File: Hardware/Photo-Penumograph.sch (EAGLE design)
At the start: 49 parts, among them SW1 SWITCH.JS202011JCQN

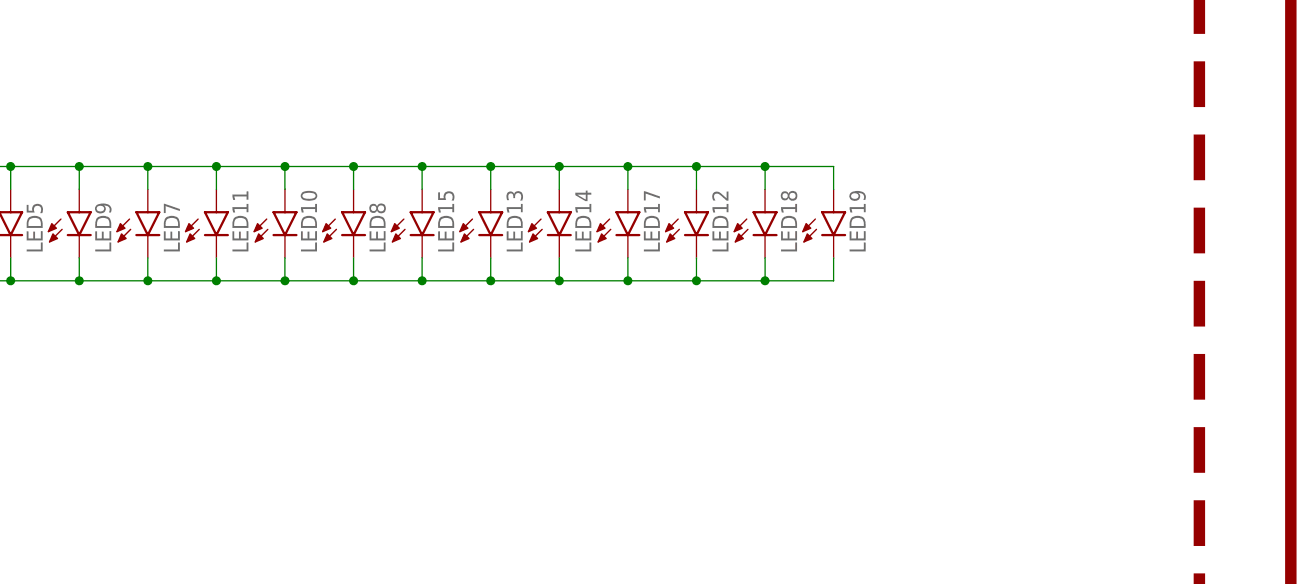
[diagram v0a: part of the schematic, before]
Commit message: Inital lung idea, doesn't expand with breath.
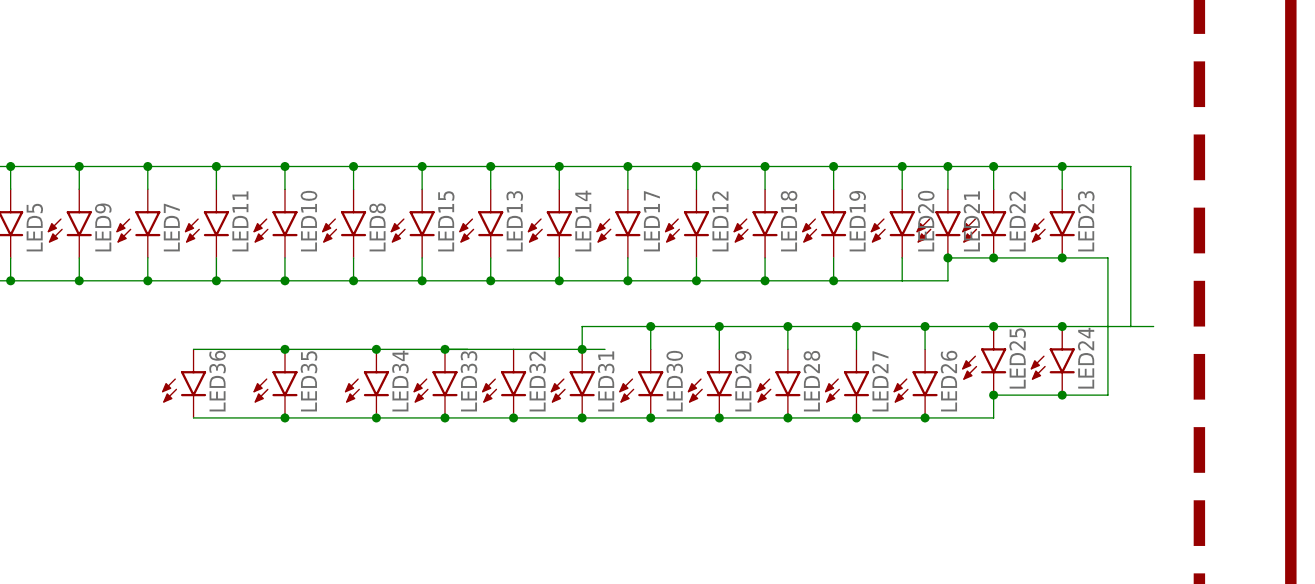
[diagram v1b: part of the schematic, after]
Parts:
- added LED20, LED21, LED22, LED23, LED24, LED25, LED26, LED27, LED28, LED29, LED30, LED31, LED32, LED33, LED34, LED35, LED36: (no value), SparkFun-LED:LED5MM
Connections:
- net ANODE: now also LED20.A, LED21.A, LED22.A, LED23.A, LED24.A, LED25.A, LED26.A, LED27.A, LED28.A, LED29.A, LED30.A, LED32.A, LED33.A, LED34.A, LED35.A, LED36.A
- net GND: now also LED20.C, LED21.C, LED22.C, LED23.C, LED24.C, LED25.C, LED26.C, LED27.C, LED28.C, LED29.C, LED30.C, LED31.C, LED32.C, LED33.C, LED34.C, LED35.C, LED36.C
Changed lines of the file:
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@@
 <?xml version="1.0" encoding="utf-8"?>
 <!DOCTYPE eagle SYSTEM "eagle.dtd">
-<eagle version="8.2.1">
+<eagle version="8.2.0">
 <drawing>
 <settings>
@@
 <part name="SUPPLY6" library="CalvEngIO-Symbols" deviceset="3.3V" device=""/>
 <part name="SUPPLY7" library="CalvEngIO-Symbols" deviceset="3.3V" device=""/>
+<part name="LED20" library="SparkFun-LED" deviceset="LED" device="5MM"/>
+<part name="LED21" library="SparkFun-LED" deviceset="LED" device="5MM"/>
+<part name="LED22" library="SparkFun-LED" deviceset="LED" device="5MM"/>
+<part name="LED23" library="SparkFun-LED" deviceset="LED" device="5MM"/>
+<part name="LED24" library="SparkFun-LED" deviceset="LED" device="5MM"/>
+<part name="LED25" library="SparkFun-LED" deviceset="LED" device="5MM"/>
+<part name="LED26" library="SparkFun-LED" deviceset="LED" device="5MM"/>
+<part name="LED27" library="SparkFun-LED" deviceset="LED" device="5MM"/>
+<part name="LED28" library="SparkFun-LED" deviceset="LED" device="5MM"/>
+<part name="LED29" library="SparkFun-LED" deviceset="LED" device="5MM"/>
+<part name="LED30" library="SparkFun-LED" deviceset="LED" device="5MM"/>
+<part name="LED31" library="SparkFun-LED" deviceset="LED" device="5MM"/>
+<part name="LED32" library="SparkFun-LED" deviceset="LED" device="5MM"/>
+<part name="LED33" library="SparkFun-LED" deviceset="LED" device="5MM"/>
+<part name="LED34" library="SparkFun-LED" deviceset="LED" device="5MM"/>
+<part name="LED35" library="SparkFun-LED" deviceset="LED" device="5MM"/>
+<part name="LED36" library="SparkFun-LED" deviceset="LED" device="5MM"/>
 </parts>
 <sheets>
@@
 <instance part="SUPPLY6" gate="G$1" x="7.62" y="93.98"/>
 <instance part="SUPPLY7" gate="G$1" x="35.56" y="91.44"/>
+<instance part="LED20" gate="G$1" x="358.14" y="73.66"/>
+<instance part="LED21" gate="G$1" x="363.22" y="73.66"/>
+<instance part="LED22" gate="G$1" x="368.3" y="73.66"/>
+<instance part="LED23" gate="G$1" x="375.92" y="73.66"/>
+<instance part="LED24" gate="G$1" x="375.92" y="58.42"/>
+<instance part="LED25" gate="G$1" x="368.3" y="58.42"/>
+<instance part="LED26" gate="G$1" x="360.68" y="55.88"/>
+<instance part="LED27" gate="G$1" x="353.06" y="55.88"/>
+<instance part="LED28" gate="G$1" x="345.44" y="55.88"/>
+<instance part="LED29" gate="G$1" x="337.82" y="55.88"/>
+<instance part="LED30" gate="G$1" x="330.2" y="55.88"/>
+<instance part="LED31" gate="G$1" x="322.58" y="55.88"/>
+<instance part="LED32" gate="G$1" x="314.96" y="55.88"/>
+<instance part="LED33" gate="G$1" x="307.34" y="55.88"/>
+<instance part="LED34" gate="G$1" x="299.72" y="55.88"/>
+<instance part="LED35" gate="G$1" x="289.56" y="55.88"/>
+<instance part="LED36" gate="G$1" x="279.4" y="55.88"/>
 </instances>
 <busses>
@@
 <wire x1="220.98" y1="58.42" x2="220.98" y2="66.04" width="0.1524" layer="91"/>
 <junction x="220.98" y="66.04"/>
+<pinref part="LED20" gate="G$1" pin="C"/>
+<wire x1="358.14" y1="68.58" x2="358.14" y2="66.04" width="0.1524" layer="91"/>
+<junction x="350.52" y="66.04"/>
+<wire x1="358.14" y1="66.04" x2="350.52" y2="66.04" width="0.1524" layer="91"/>
+<wire x1="363.22" y1="66.04" x2="358.14" y2="66.04" width="0.1524" layer="91"/>
+<pinref part="LED24" gate="G$1" pin="C"/>
+<wire x1="375.92" y1="53.34" x2="381" y2="53.34" width="0.1524" layer="91"/>
+<wire x1="381" y1="53.34" x2="381" y2="68.58" width="0.1524" layer="91"/>
+<pinref part="LED23" gate="G$1" pin="C"/>
+<wire x1="381" y1="68.58" x2="375.92" y2="68.58" width="0.1524" layer="91"/>
+<pinref part="LED22" gate="G$1" pin="C"/>
+<wire x1="375.92" y1="68.58" x2="368.3" y2="68.58" width="0.1524" layer="91"/>
+<junction x="375.92" y="68.58"/>
+<pinref part="LED21" gate="G$1" pin="C"/>
+<wire x1="368.3" y1="68.58" x2="363.22" y2="68.58" width="0.1524" layer="91"/>
+<junction x="368.3" y="68.58"/>
+<wire x1="363.22" y1="66.04" x2="363.22" y2="68.58" width="0.1524" layer="91"/>
+<junction x="363.22" y="68.58"/>
+<pinref part="LED25" gate="G$1" pin="C"/>
+<wire x1="375.92" y1="53.34" x2="368.3" y2="53.34" width="0.1524" layer="91"/>
+<junction x="375.92" y="53.34"/>
+<wire x1="368.3" y1="53.34" x2="368.3" y2="50.8" width="0.1524" layer="91"/>
+<junction x="368.3" y="53.34"/>
+<pinref part="LED26" gate="G$1" pin="C"/>
+<wire x1="368.3" y1="50.8" x2="360.68" y2="50.8" width="0.1524" layer="91"/>
+<pinref part="LED27" gate="G$1" pin="C"/>
+<wire x1="360.68" y1="50.8" x2="353.06" y2="50.8" width="0.1524" layer="91"/>
+<junction x="360.68" y="50.8"/>
+<pinref part="LED28" gate="G$1" pin="C"/>
+<wire x1="353.06" y1="50.8" x2="345.44" y2="50.8" width="0.1524" layer="91"/>
+<junction x="353.06" y="50.8"/>
+<pinref part="LED29" gate="G$1" pin="C"/>
+<wire x1="345.44" y1="50.8" x2="337.82" y2="50.8" width="0.1524" layer="91"/>
+<junction x="345.44" y="50.8"/>
+<pinref part="LED30" gate="G$1" pin="C"/>
+<wire x1="337.82" y1="50.8" x2="330.2" y2="50.8" width="0.1524" layer="91"/>
+<junction x="337.82" y="50.8"/>
+<pinref part="LED31" gate="G$1" pin="C"/>
+<wire x1="330.2" y1="50.8" x2="322.58" y2="50.8" width="0.1524" layer="91"/>
+<junction x="330.2" y="50.8"/>
+<pinref part="LED32" gate="G$1" pin="C"/>
+<wire x1="322.58" y1="50.8" x2="314.96" y2="50.8" width="0.1524" layer="91"/>
+<junction x="322.58" y="50.8"/>
+<pinref part="LED33" gate="G$1" pin="C"/>
+<wire x1="314.96" y1="50.8" x2="307.34" y2="50.8" width="0.1524" layer="91"/>
+<junction x="314.96" y="50.8"/>
+<pinref part="LED34" gate="G$1" pin="C"/>
+<wire x1="307.34" y1="50.8" x2="299.72" y2="50.8" width="0.1524" layer="91"/>
+<junction x="307.34" y="50.8"/>
+<pinref part="LED35" gate="G$1" pin="C"/>
+<wire x1="299.72" y1="50.8" x2="289.56" y2="50.8" width="0.1524" layer="91"/>
+<junction x="299.72" y="50.8"/>
+<pinref part="LED36" gate="G$1" pin="C"/>
+<wire x1="289.56" y1="50.8" x2="279.4" y2="50.8" width="0.1524" layer="91"/>
+<junction x="289.56" y="50.8"/>
 </segment>
 <segment>
@@
 <wire x1="220.98" y1="81.28" x2="220.98" y2="78.74" width="0.1524" layer="91"/>
 <junction x="220.98" y="78.74"/>
+<pinref part="LED20" gate="G$1" pin="A"/>
+<wire x1="350.52" y1="78.74" x2="358.14" y2="78.74" width="0.1524" layer="91"/>
+<wire x1="358.14" y1="78.74" x2="358.14" y2="76.2" width="0.1524" layer="91"/>
+<junction x="350.52" y="78.74"/>
+<pinref part="LED21" gate="G$1" pin="A"/>
+<wire x1="363.22" y1="76.2" x2="363.22" y2="78.74" width="0.1524" layer="91"/>
+<wire x1="363.22" y1="78.74" x2="358.14" y2="78.74" width="0.1524" layer="91"/>
+<junction x="358.14" y="78.74"/>
+<pinref part="LED22" gate="G$1" pin="A"/>
+<wire x1="368.3" y1="76.2" x2="368.3" y2="78.74" width="0.1524" layer="91"/>
+<wire x1="368.3" y1="78.74" x2="363.22" y2="78.74" width="0.1524" layer="91"/>
+<junction x="363.22" y="78.74"/>
+<pinref part="LED23" gate="G$1" pin="A"/>
+<wire x1="375.92" y1="76.2" x2="375.92" y2="78.74" width="0.1524" layer="91"/>
+<wire x1="375.92" y1="78.74" x2="368.3" y2="78.74" width="0.1524" layer="91"/>
+<junction x="368.3" y="78.74"/>
+<pinref part="LED24" gate="G$1" pin="A"/>
+<wire x1="375.92" y1="60.96" x2="383.54" y2="60.96" width="0.1524" layer="91"/>
+<wire x1="386.08" y1="60.96" x2="383.54" y2="60.96" width="0.1524" layer="91"/>
+<wire x1="383.54" y1="60.96" x2="383.54" y2="78.74" width="0.1524" layer="91"/>
+<wire x1="383.54" y1="78.74" x2="375.92" y2="78.74" width="0.1524" layer="91"/>
+<junction x="375.92" y="78.74"/>
+<pinref part="LED25" gate="G$1" pin="A"/>
+<wire x1="368.3" y1="60.96" x2="375.92" y2="60.96" width="0.1524" layer="91"/>
+<junction x="375.92" y="60.96"/>
+<pinref part="LED26" gate="G$1" pin="A"/>
+<wire x1="360.68" y1="58.42" x2="360.68" y2="60.96" width="0.1524" layer="91"/>
+<wire x1="360.68" y1="60.96" x2="368.3" y2="60.96" width="0.1524" layer="91"/>
+<junction x="368.3" y="60.96"/>
+<pinref part="LED27" gate="G$1" pin="A"/>
+<wire x1="353.06" y1="58.42" x2="353.06" y2="60.96" width="0.1524" layer="91"/>
+<wire x1="353.06" y1="60.96" x2="360.68" y2="60.96" width="0.1524" layer="91"/>
+<junction x="360.68" y="60.96"/>
+<pinref part="LED28" gate="G$1" pin="A"/>
+<wire x1="345.44" y1="58.42" x2="345.44" y2="60.96" width="0.1524" layer="91"/>
+<wire x1="345.44" y1="60.96" x2="353.06" y2="60.96" width="0.1524" layer="91"/>
+<junction x="353.06" y="60.96"/>
+<pinref part="LED29" gate="G$1" pin="A"/>
+<wire x1="337.82" y1="58.42" x2="337.82" y2="60.96" width="0.1524" layer="91"/>
+<wire x1="337.82" y1="60.96" x2="345.44" y2="60.96" width="0.1524" layer="91"/>
+<junction x="345.44" y="60.96"/>
+<pinref part="LED30" gate="G$1" pin="A"/>
+<wire x1="330.2" y1="58.42" x2="330.2" y2="60.96" width="0.1524" layer="91"/>
+<wire x1="330.2" y1="60.96" x2="337.82" y2="60.96" width="0.1524" layer="91"/>
+<junction x="337.82" y="60.96"/>
+<pinref part="LED36" gate="G$1" pin="A"/>
+<pinref part="LED35" gate="G$1" pin="A"/>
+<wire x1="279.4" y1="58.42" x2="289.56" y2="58.42" width="0.1524" layer="91"/>
+<pinref part="LED34" gate="G$1" pin="A"/>
+<wire x1="289.56" y1="58.42" x2="299.72" y2="58.42" width="0.1524" layer="91"/>
+<junction x="289.56" y="58.42"/>
+<wire x1="299.72" y1="58.42" x2="307.34" y2="58.42" width="0.1524" layer="91"/>
+<junction x="299.72" y="58.42"/>
+<pinref part="LED33" gate="G$1" pin="A"/>
+<wire x1="309.88" y1="58.42" x2="307.34" y2="58.42" width="0.1524" layer="91"/>
+<junction x="307.34" y="58.42"/>
+<pinref part="LED32" gate="G$1" pin="A"/>
+<wire x1="314.96" y1="58.42" x2="322.58" y2="58.42" width="0.1524" layer="91"/>
+<wire x1="322.58" y1="58.42" x2="325.12" y2="58.42" width="0.1524" layer="91"/>
+<wire x1="314.96" y1="58.42" x2="307.34" y2="58.42" width="0.1524" layer="91"/>
+<wire x1="322.58" y1="58.42" x2="322.58" y2="60.96" width="0.1524" layer="91"/>
+<junction x="322.58" y="58.42"/>
+<wire x1="322.58" y1="60.96" x2="330.2" y2="60.96" width="0.1524" layer="91"/>
+<junction x="330.2" y="60.96"/>
 </segment>
 </net>

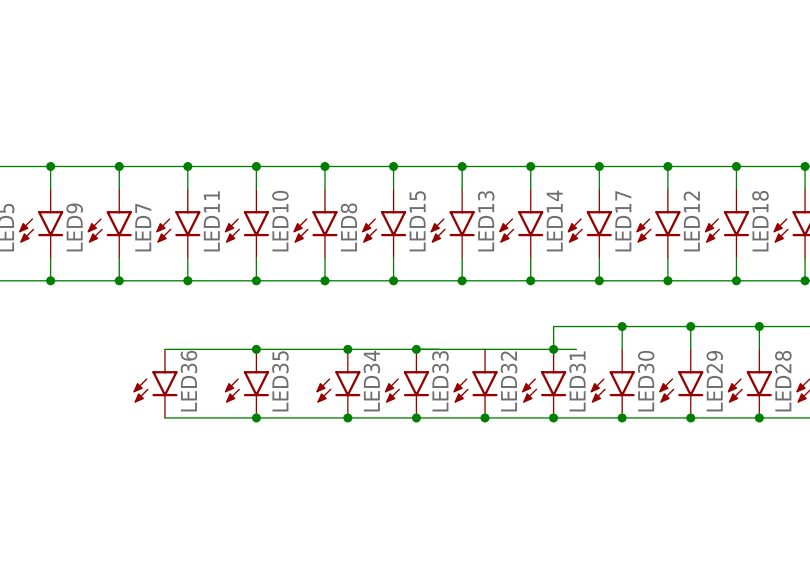
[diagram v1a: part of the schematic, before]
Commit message: Improved basic lung design
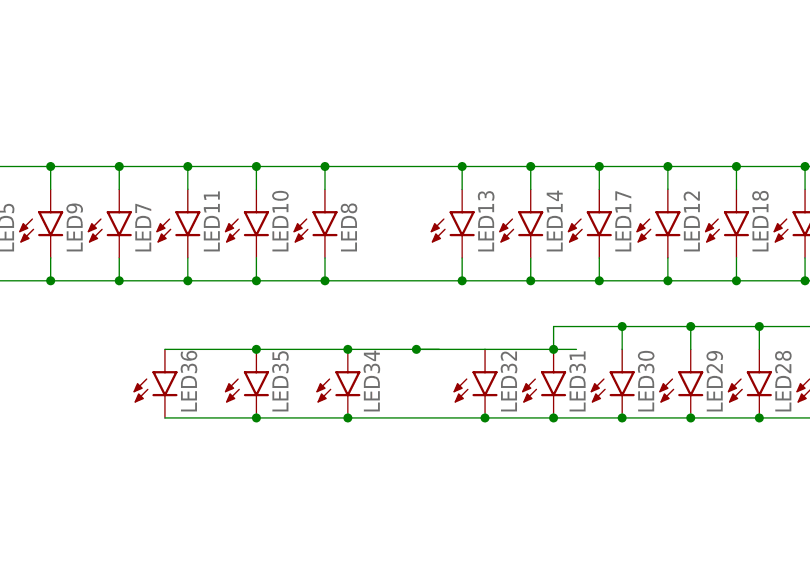
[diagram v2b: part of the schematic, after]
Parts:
- removed LED15, LED33: (no value), SparkFun-LED:LED5MM
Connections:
- net ANODE: no longer LED15.A, LED33.A
- net GND: no longer LED15.C, LED33.C
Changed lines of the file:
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@@
 <part name="LED14" library="SparkFun-LED" deviceset="LED" device="5MM"/>
 <part name="LED13" library="SparkFun-LED" deviceset="LED" device="5MM"/>
-<part name="LED15" library="SparkFun-LED" deviceset="LED" device="5MM"/>
 <part name="LED17" library="SparkFun-LED" deviceset="LED" device="5MM"/>
 <part name="LED18" library="SparkFun-LED" deviceset="LED" device="5MM"/>
@@
 <part name="LED31" library="SparkFun-LED" deviceset="LED" device="5MM"/>
 <part name="LED32" library="SparkFun-LED" deviceset="LED" device="5MM"/>
-<part name="LED33" library="SparkFun-LED" deviceset="LED" device="5MM"/>
 <part name="LED34" library="SparkFun-LED" deviceset="LED" device="5MM"/>
 <part name="LED35" library="SparkFun-LED" deviceset="LED" device="5MM"/>
@@
 <instance part="LED14" gate="G$1" x="320.04" y="73.66"/>
 <instance part="LED13" gate="G$1" x="312.42" y="73.66"/>
-<instance part="LED15" gate="G$1" x="304.8" y="73.66"/>
 <instance part="LED17" gate="G$1" x="327.66" y="73.66"/>
 <instance part="LED18" gate="G$1" x="342.9" y="73.66"/>
@@
 <instance part="LED31" gate="G$1" x="322.58" y="55.88"/>
 <instance part="LED32" gate="G$1" x="314.96" y="55.88"/>
-<instance part="LED33" gate="G$1" x="307.34" y="55.88"/>
 <instance part="LED34" gate="G$1" x="299.72" y="55.88"/>
 <instance part="LED35" gate="G$1" x="289.56" y="55.88"/>
@@
 <wire x1="281.94" y1="66.04" x2="289.56" y2="66.04" width="0.1524" layer="91"/>
 <wire x1="289.56" y1="66.04" x2="297.18" y2="66.04" width="0.1524" layer="91"/>
-<wire x1="297.18" y1="66.04" x2="304.8" y2="66.04" width="0.1524" layer="91"/>
-<wire x1="304.8" y1="66.04" x2="312.42" y2="66.04" width="0.1524" layer="91"/>
+<wire x1="297.18" y1="66.04" x2="312.42" y2="66.04" width="0.1524" layer="91"/>
 <wire x1="312.42" y1="66.04" x2="320.04" y2="66.04" width="0.1524" layer="91"/>
 <wire x1="320.04" y1="66.04" x2="327.66" y2="66.04" width="0.1524" layer="91"/>
@@
 <wire x1="297.18" y1="68.58" x2="297.18" y2="66.04" width="0.1524" layer="91"/>
 <junction x="297.18" y="66.04"/>
-<pinref part="LED15" gate="G$1" pin="C"/>
-<wire x1="304.8" y1="68.58" x2="304.8" y2="66.04" width="0.1524" layer="91"/>
-<junction x="304.8" y="66.04"/>
 <pinref part="LED13" gate="G$1" pin="C"/>
 <wire x1="312.42" y1="68.58" x2="312.42" y2="66.04" width="0.1524" layer="91"/>
@@
 <wire x1="322.58" y1="50.8" x2="314.96" y2="50.8" width="0.1524" layer="91"/>
 <junction x="322.58" y="50.8"/>
-<pinref part="LED33" gate="G$1" pin="C"/>
-<wire x1="314.96" y1="50.8" x2="307.34" y2="50.8" width="0.1524" layer="91"/>
 <junction x="314.96" y="50.8"/>
 <pinref part="LED34" gate="G$1" pin="C"/>
-<wire x1="307.34" y1="50.8" x2="299.72" y2="50.8" width="0.1524" layer="91"/>
-<junction x="307.34" y="50.8"/>
+<wire x1="314.96" y1="50.8" x2="299.72" y2="50.8" width="0.1524" layer="91"/>
 <pinref part="LED35" gate="G$1" pin="C"/>
 <wire x1="299.72" y1="50.8" x2="289.56" y2="50.8" width="0.1524" layer="91"/>
@@
 <wire x1="281.94" y1="78.74" x2="289.56" y2="78.74" width="0.1524" layer="91"/>
 <wire x1="289.56" y1="78.74" x2="297.18" y2="78.74" width="0.1524" layer="91"/>
-<wire x1="297.18" y1="78.74" x2="304.8" y2="78.74" width="0.1524" layer="91"/>
-<wire x1="304.8" y1="78.74" x2="312.42" y2="78.74" width="0.1524" layer="91"/>
+<wire x1="297.18" y1="78.74" x2="312.42" y2="78.74" width="0.1524" layer="91"/>
 <wire x1="312.42" y1="78.74" x2="320.04" y2="78.74" width="0.1524" layer="91"/>
 <wire x1="320.04" y1="78.74" x2="327.66" y2="78.74" width="0.1524" layer="91"/>
@@
 <wire x1="312.42" y1="76.2" x2="312.42" y2="78.74" width="0.1524" layer="91"/>
 <junction x="312.42" y="78.74"/>
-<pinref part="LED15" gate="G$1" pin="A"/>
-<wire x1="304.8" y1="76.2" x2="304.8" y2="78.74" width="0.1524" layer="91"/>
-<junction x="304.8" y="78.74"/>
 <pinref part="LED8" gate="G$1" pin="A"/>
 <wire x1="297.18" y1="76.2" x2="297.18" y2="78.74" width="0.1524" layer="91"/>
@@
 <wire x1="299.72" y1="58.42" x2="307.34" y2="58.42" width="0.1524" layer="91"/>
 <junction x="299.72" y="58.42"/>
-<pinref part="LED33" gate="G$1" pin="A"/>
 <wire x1="309.88" y1="58.42" x2="307.34" y2="58.42" width="0.1524" layer="91"/>
 <junction x="307.34" y="58.42"/>
